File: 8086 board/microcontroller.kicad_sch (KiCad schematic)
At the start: 13 parts, among them U33 ATmega328P, U34 74HC595, U35 74HC595, U36 74HC595, U37 74HC165, U38 74HC165, Y1 16MHz

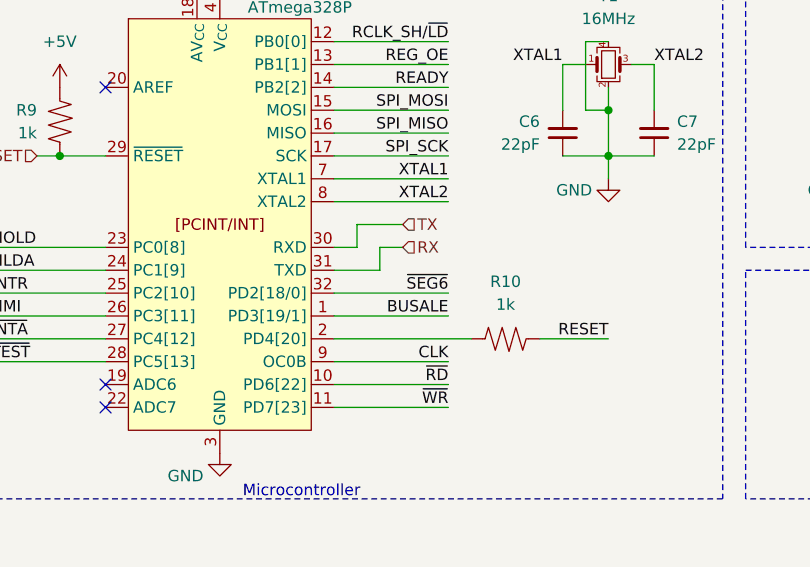
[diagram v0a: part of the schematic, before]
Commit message: change schematic to use new components
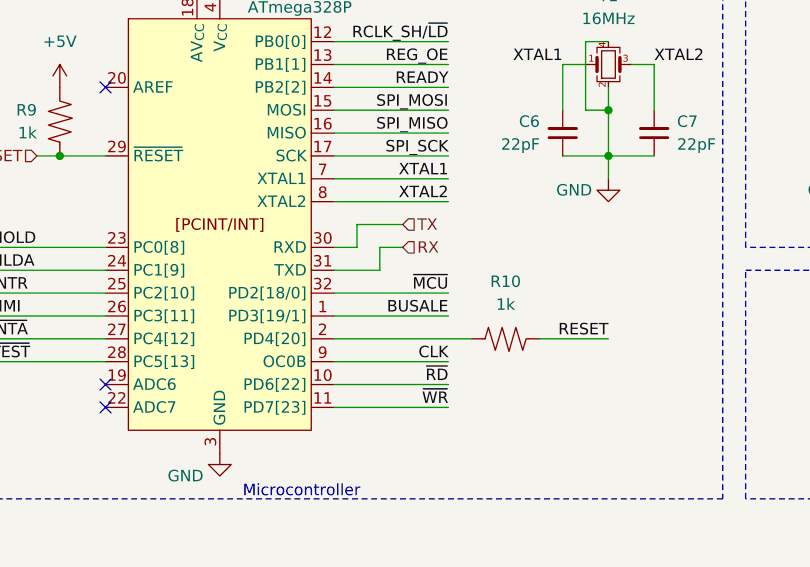
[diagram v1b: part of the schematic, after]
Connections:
- net ~{SEG6} renamed ~{MCU}
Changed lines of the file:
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@@
   (title_block
     (title "8086 computer")
-    (date "2023.10.26")
-    (rev "V1.0.0")
+    (date "2023.10.29")
+    (rev "V1.1.0")
     (company "Eldad Hellerman")
     (comment 1 "Open Source: github.com/EldadHellerman/8086-computer")
@@
     (effects (font (size 1.27 1.27)) (justify left bottom))
   )
-  (label "~{SEG6}" (at 76.2 55.88 180) (fields_autoplaced)
-    (effects (font (size 1.27 1.27)) (justify right bottom))
-  )
+  (label "~{MCU}" (at 76.2 55.88 180) (fields_autoplaced)
+    (effects (font (size 1.27 1.27)) (justify right bottom))
+  )

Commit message: schematic: reduced 8086 bus, no LCD shield
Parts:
- U34, U35, U36, U37, U38: footprint Package_SO:SOIC-16_3.9x9.9mm_P1.27mm -> Package_SO:TSSOP-16_4.4x5mm_P0.65mm
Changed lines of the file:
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@@
       (effects (font (size 1.27 1.27)) (justify left))
     )
-    (property "Footprint" "Package_SO:SOIC-16_3.9x9.9mm_P1.27mm" (at 177.8 48.26 0)
+    (property "Footprint" "Package_SO:TSSOP-16_4.4x5mm_P0.65mm" (at 177.8 48.26 0)
       (effects (font (size 1.27 1.27)) hide)
     )
@@
       (effects (font (size 1.27 1.27)))
     )
-    (property "Footprint" "Package_SO:SOIC-16_3.9x9.9mm_P1.27mm" (at 203.2 86.36 0)
+    (property "Footprint" "Package_SO:TSSOP-16_4.4x5mm_P0.65mm" (at 203.2 86.36 0)
       (effects (font (size 1.27 1.27)) hide)
     )
@@
       (effects (font (size 1.27 1.27)))
     )
-    (property "Footprint" "Package_SO:SOIC-16_3.9x9.9mm_P1.27mm" (at 241.3 86.36 0)
+    (property "Footprint" "Package_SO:TSSOP-16_4.4x5mm_P0.65mm" (at 241.3 86.36 0)
       (effects (font (size 1.27 1.27)) hide)
     )
@@
       (effects (font (size 1.27 1.27)) (justify left))
     )
-    (property "Footprint" "Package_SO:SOIC-16_3.9x9.9mm_P1.27mm" (at 220.98 48.26 0)
+    (property "Footprint" "Package_SO:TSSOP-16_4.4x5mm_P0.65mm" (at 220.98 48.26 0)
       (effects (font (size 1.27 1.27)) hide)
     )
@@
       (effects (font (size 1.27 1.27)) (justify left))
     )
-    (property "Footprint" "Package_SO:SOIC-16_3.9x9.9mm_P1.27mm" (at 264.16 48.26 0)
-      (effects (font (size 1.27 1.27)) hide)
-    )
+    (property "Footprint" "Package_SO:TSSOP-16_4.4x5mm_P0.65mm" (at 264.16 48.26 0)
+      (effects (font (size 1.27 1.27)) hide)
+    )

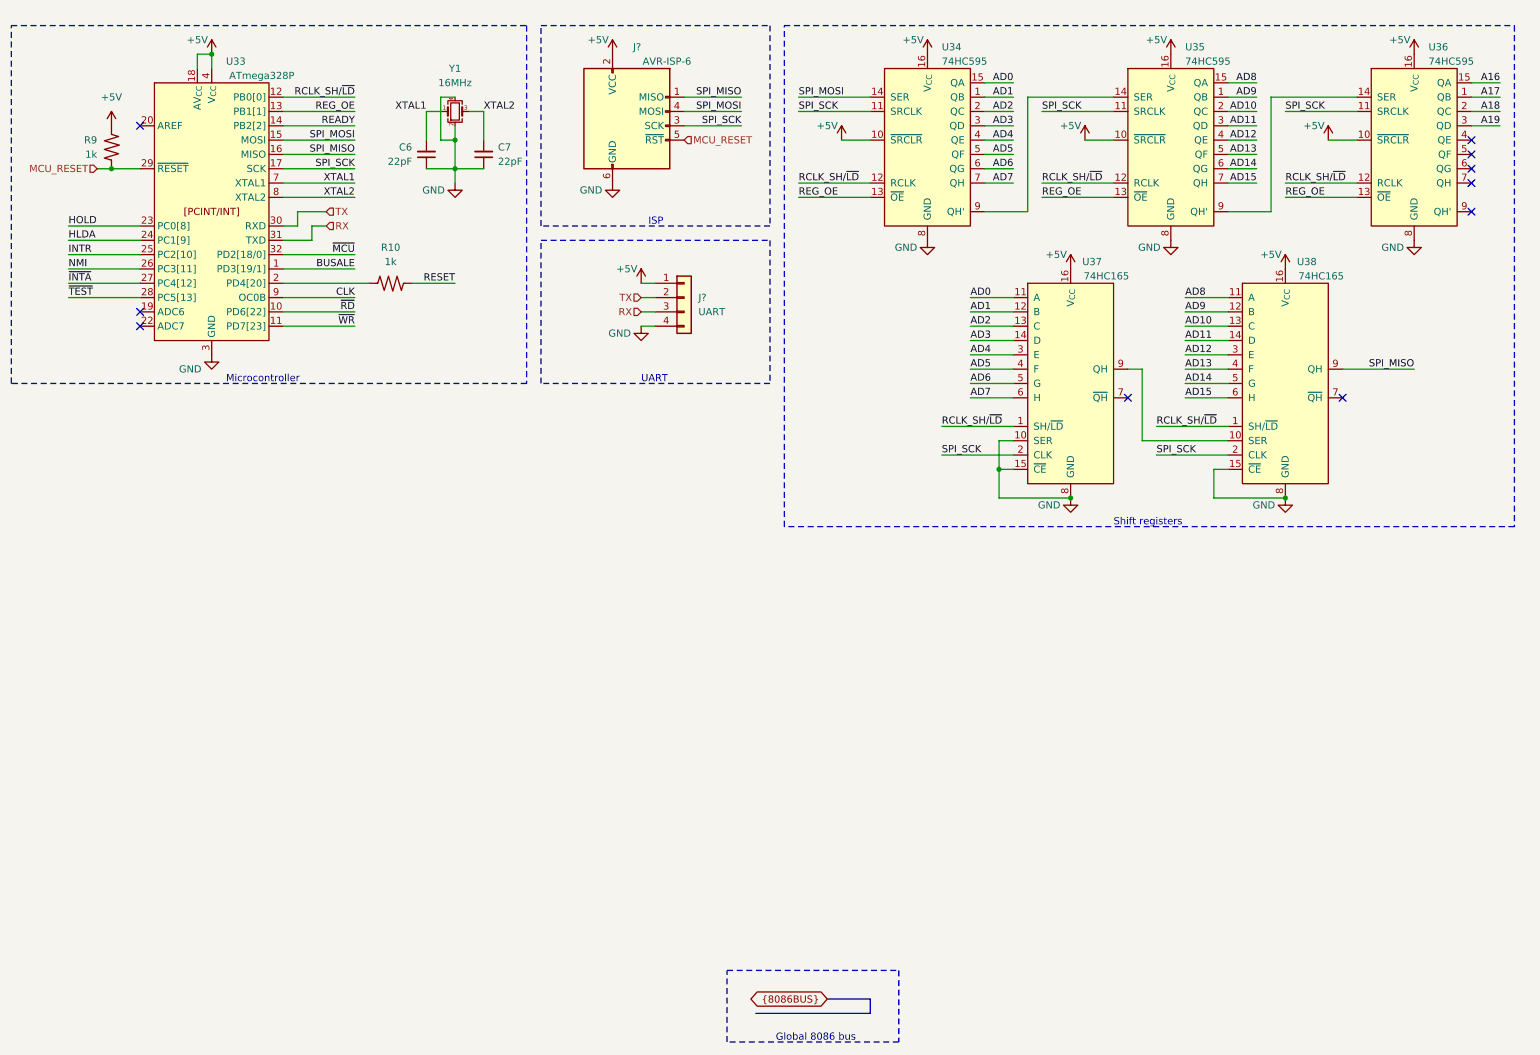
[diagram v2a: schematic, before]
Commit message: PCB: more layout work. some schematic changes.
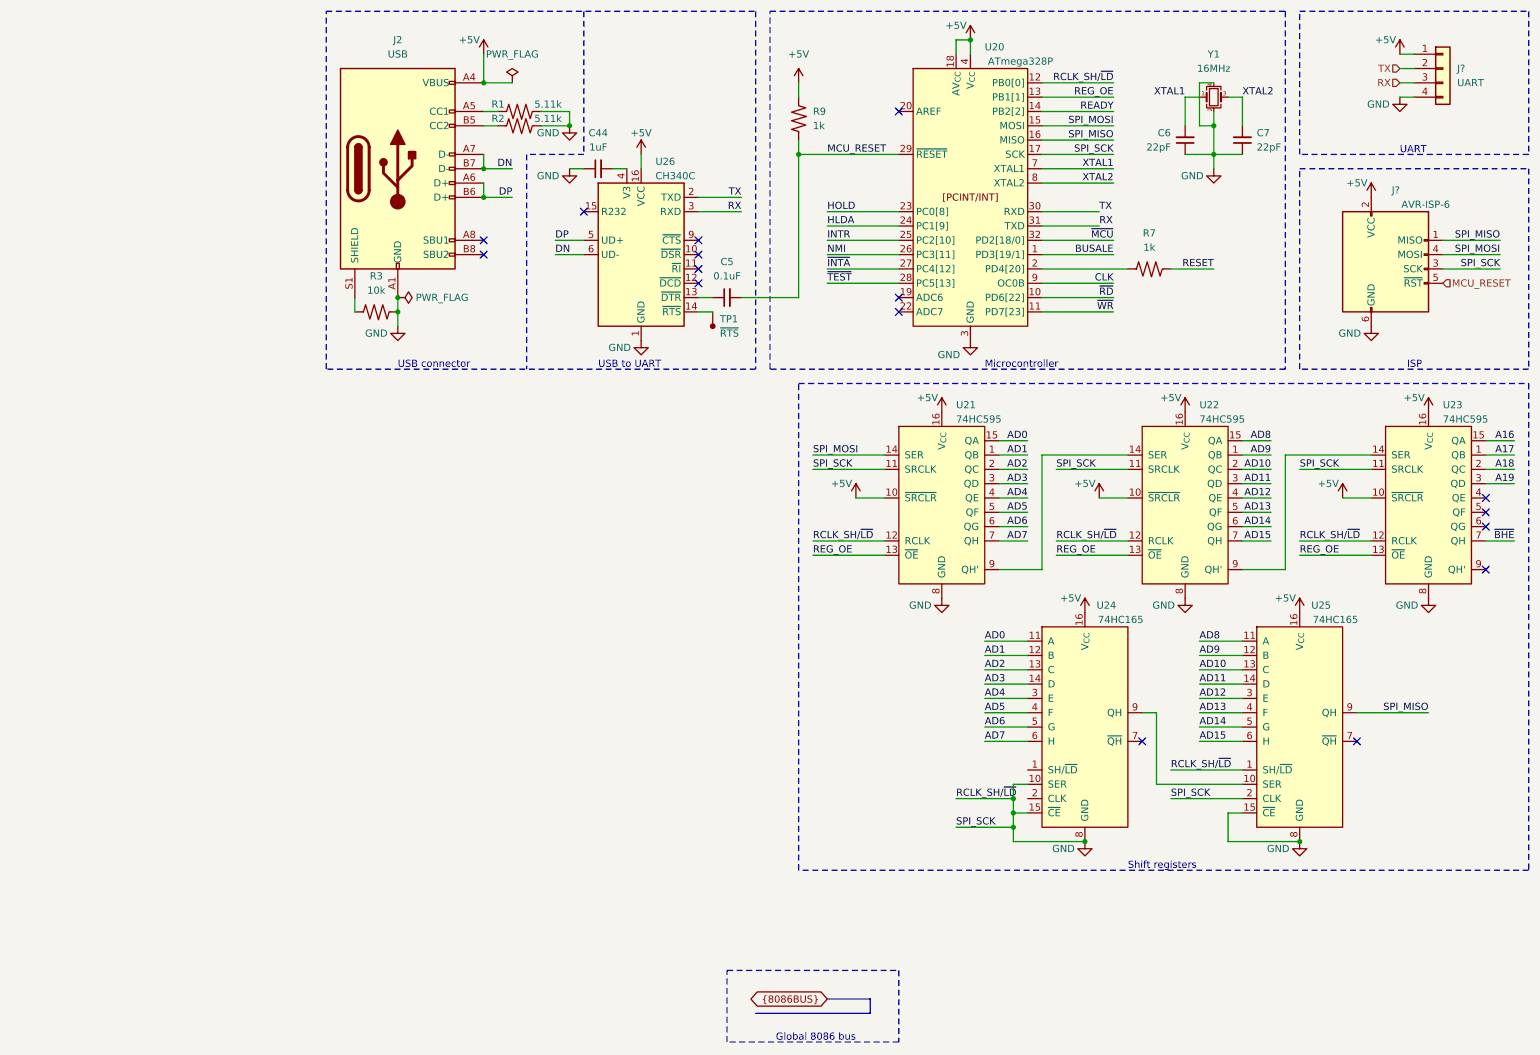
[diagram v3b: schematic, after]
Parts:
- added C44: 1uF, Capacitor_SMD:C_0603_1608Metric_Pad1.08x0.95mm_HandSolder, symbol Device:C_Small
- added C5: 0.1uF, Capacitor_SMD:C_0603_1608Metric_Pad1.08x0.95mm_HandSolder, symbol Device:C_Small
- added J2: USB, Connector_USB:USB_C_Receptacle_GCT_USB4105-xx-A_16P_TopMnt_Horizontal, symbol Connector:USB_C_Receptacle_USB2.0
- added R1, R2: 5.11k, Resistor_SMD:R_0603_1608Metric_Pad0.98x0.95mm_HandSolder, symbol 8086PC:R
- added R3: 10k, Resistor_SMD:R_0603_1608Metric_Pad0.98x0.95mm_HandSolder, symbol 8086PC:R
- added TP1: ~{RTS}, TestPoint:TestPoint_Pad_1.5x1.5mm, symbol 8086PC:TestPoint
- added U26: CH340C, Package_SO:SOIC-16_3.9x9.9mm_P1.27mm, symbol Interface_USB:CH340C
- renumbered R10 to R7, U33 to U20, U34 to U21, U35 to U22, U36 to U23, U37 to U24, U38 to U25
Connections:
- net +5V: now also J2.A4 (VBUS), J2.A9 (VBUS), J2.B4 (VBUS), J2.B9 (VBUS), U26.16 (VCC)
- net GND: now also J?.3 (SCK), U20.12 (PB0[0]), U20.17 (PB5[5]), U21.11 (SRCLK), U21.12 (RCLK), U22.11 (SRCLK), U22.12 (RCLK), U23.11 (SRCLK), U23.12 (RCLK), U25.1 (SH/~{LD}), U25.2 (CLK), C44.1, J2.A1 (GND), J2.A12 (GND), J2.B1 (GND), J2.B12 (GND), R1.2, R2.2, R3.2, U26.1 (GND)
- net MCU_RESET: now also C5.2
- net RX: now also U26.3 (RXD)
- net TX: now also U26.2 (TXD)
- net ~{BHE}: now reaches U23.7 (QH)
- removed net RCLK_SH/~{LD}: U20.12 (PB0[0]), U21.12 (RCLK), U22.12 (RCLK), U23.12 (RCLK), U24.1 (SH/~{LD}), U25.1 (SH/~{LD})
- removed net SPI_SCK: J?.3 (SCK), U20.17 (PB5[5]), U21.11 (SRCLK), U22.11 (SRCLK), U23.11 (SRCLK), U24.2 (CLK), U25.2 (CLK)
- new net: J2.S1 (SHIELD), R3.1
- new net: C44.2, U26.4 (V3)
- new net: C5.1, U26.13 (~{DTR})
- new net: TP1.1, U26.14 (~{RTS})
- new net: J2.A5 (CC1), R1.1
- new net: J2.B5 (CC2), R2.1
- new net DN: J2.A7 (D-), J2.B7 (D-), U26.6 (UD-)
- new net DP: J2.A6 (D+), J2.B6 (D+), U26.5 (UD+)
- no-connect marks 10 -> 16
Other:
- note added: "USB connector"
- note added: "USB to UART"
- moved on the sheet: C6, C7, J?, R7, R9, U20, U21, U22, U23, U24, U25, Y1
